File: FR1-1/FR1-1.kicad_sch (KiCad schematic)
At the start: 32 parts

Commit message: cleaning up references
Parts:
- renumbered 1A_FR1_ to 1A_FR1, 1A_FR2_ to 1A_FR2, 1B_FR1_ to 1B_FR1, 1B_FR2_ to 1B_FR2, 1C_FR1_ to 1C_FR1, 1C_FR2_ to 1C_FR2, 1D_FR1_ to 1D_FR1, 1D_FR2_ to 1D_FR2, 1E_FR1_ to 1E_FR1, 1E_FR2_ to 1E_FR2, 3A_FR1_ to 3A_FR1, 3A_FR2_ to 3A_FR2, 3B_FR1_ to 3B_FR1, 3B_FR2_ to 3B_FR2, 3C_FR1_ to 3C_FR1, 3C_FR2_ to 3C_FR2, 3E_FR1_ to 3E_FR1, 3E_FR2_ to 3E_FR2, 3F_FR1_ to 3F_FR1, 3F_FR2_ to 3F_FR2, 5A_FR1_1 to 5A_FR1, 5A_FR2_ to 5A_FR2, 5B_FR1_1 to 5B_FR1, 5B_FR2_ to 5B_FR2, 5C_FR1_1 to 5C_FR1, 5C_FR2_ to 5C_FR2, 5E_FR1_ to 5E_FR1, 5E_FR2_ to 5E_FR2, 5F_FR1_ to 5F_FR1, 5F_FR2_ to 5F_FR2

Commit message: Some initial fixing of ERC errors.
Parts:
- added unit 2 of 5A_FR1
- added unit 2 of 5B_FR1
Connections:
- net GND: now also 5A_FR1.7 (GND), 5B_FR1.7 (GND)
- net VCC: now also 5A_FR1.14 (VCC), 5B_FR1.14 (VCC)

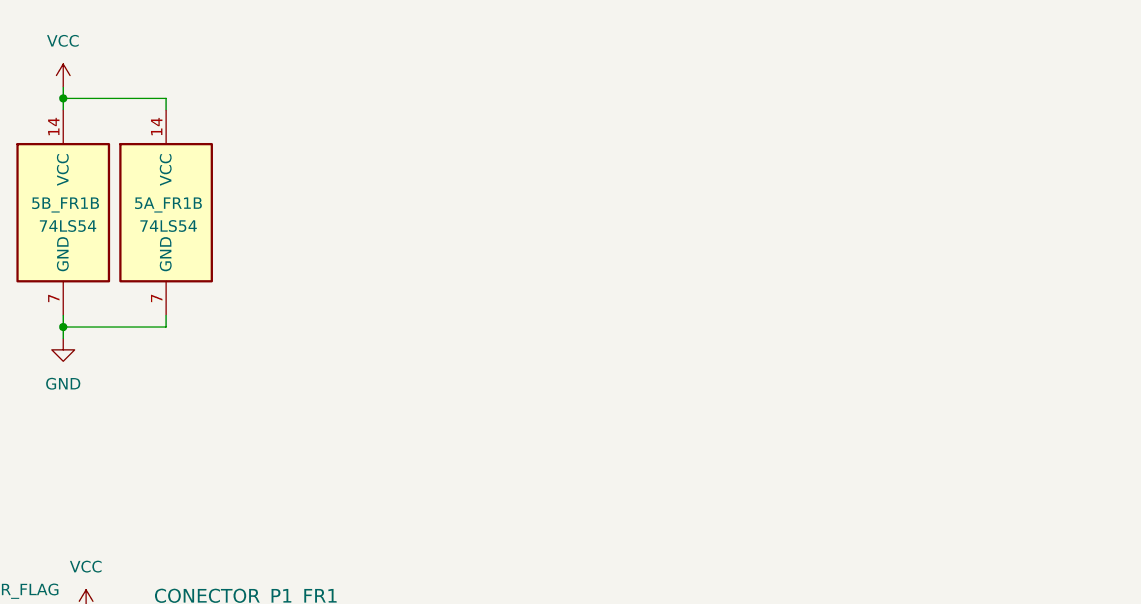
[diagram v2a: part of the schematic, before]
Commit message: addressing a few more ERC errors
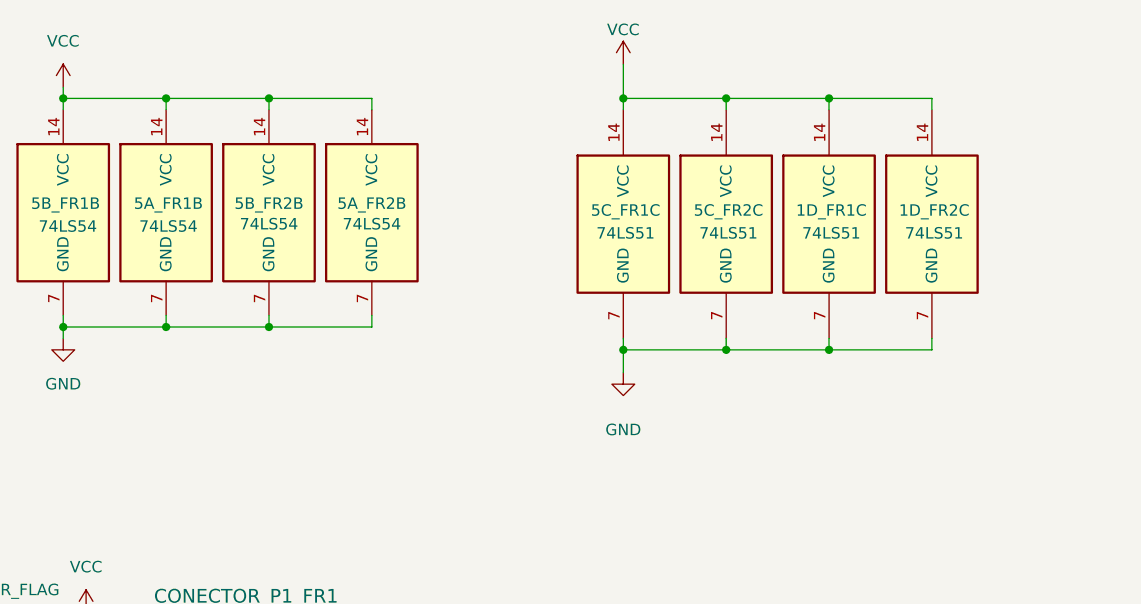
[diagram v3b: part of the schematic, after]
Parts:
- added unit 3 of 1D_FR1
- added unit 3 of 1D_FR2
- added unit 2 of 5A_FR2
- added unit 2 of 5B_FR2
- added unit 3 of 5C_FR1
- added unit 3 of 5C_FR2
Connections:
- net GND: now also 1D_FR1.7 (GND), 1D_FR2.7 (GND), 5A_FR2.7 (GND), 5B_FR2.7 (GND), 5C_FR1.7 (GND), 5C_FR2.7 (GND)
- net VCC: now also 1D_FR1.14 (VCC), 1D_FR2.14 (VCC), 5A_FR2.14 (VCC), 5B_FR2.14 (VCC), 5C_FR1.14 (VCC), 5C_FR2.14 (VCC)

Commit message: fix a whole bunch of errors
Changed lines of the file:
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@@
 	)
 	(junction
-		(at 45.72 22.86)
-		(diameter 0)
-		(color 0 0 0 0)
-	)
-	(junction
 		(at 217.17 157.48)
 		(diameter 0)
@@
 	(wire
 		(pts
-			(xy 38.1 22.86) (xy 45.72 22.86)
-		)
-		(stroke
-			(width 0)
-			(type default)
-		)
-	)
-	(wire
-		(pts
 			(xy 298.45 125.73) (xy 298.45 93.98)
 		)
@@
 	(wire
 		(pts
-			(xy 38.1 21.59) (xy 38.1 22.86)
-		)
-		(stroke
-			(width 0)
-			(type default)
-		)
-	)
-	(wire
-		(pts
 			(xy 374.65 66.04) (xy 374.65 83.82)
 		)
@@
 					(unit 1)
 				)
-			)
-		)
-	)
-	(symbol
-		(lib_id "power:PWR_FLAG")
-		(at 38.1 21.59 0)
-		(unit 1)
-		(body_style 1)
-		(exclude_from_sim no)
-		(in_bom yes)
-		(on_board yes)
-		(in_pos_files yes)
-		(dnp no)
-		(fields_autoplaced yes)
-		(property "Reference" "#FLG07"
-			(at 38.1 19.685 0)
-			(hide yes)
-			(show_name no)
-			(do_not_autoplace no)
-			(effects
-				(font
-					(size 1.27 1.27)
-				)
-			)
-		)
-		(property "Value" "PWR_FLAG"
-			(at 38.1 16.51 0)
-			(show_name no)
-			(do_not_autoplace no)
-			(effects
-				(font
-					(size 1.27 1.27)
-				)
-			)
-		)
-		(property "Footprint" ""
-			(at 38.1 21.59 0)
-			(hide yes)
-			(show_name no)
-			(do_not_autoplace no)
-			(effects
-				(font
-					(size 1.27 1.27)
-				)
-			)
-		)
-		(property "Datasheet" ""
-			(at 38.1 21.59 0)
-			(hide yes)
-			(show_name no)
-			(do_not_autoplace no)
-			(effects
-				(font
-					(size 1.27 1.27)
-				)
-			)
-		)
-		(property "Description" "Special symbol for telling ERC where power comes from"
-			(at 38.1 21.59 0)
-			(hide yes)
-			(show_name no)
-			(do_not_autoplace no)
-			(effects
-				(font
-					(size 1.27 1.27)
-				)
-			)
-		)
-		(pin "1"
-		)
-		(instances
-			(project "patinhofeio"
-				(path "/aca06203-542d-4682-a7e3-8839e24cce95/b383f260-e697-4084-9247-6984c2eebf73"
-					(reference "#FLG07")
-					(unit 1)
-				)

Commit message: melhorias dessa semana
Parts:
- removed 1E_FR1, 1E_FR2: 7400, Housings_DIP:DIP-14_W7.62mm_Socket_LongPads, symbol CDE-3-rescue:7400-RESCUE-CDE-3
- removed 3E_FR1, 3E_FR2, 3F_FR1, 3F_FR2, 5E_FR1, 5E_FR2, 5F_FR1, 5F_FR2: 74HC74, symbol CCE-2-rescue:74HC74
- added 1E_FR1, 1E_FR2: 74LS00, symbol 74xx:74LS00
- added 3E_FR1, 3E_FR2, 3F_FR1, 3F_FR2, 5E_FR1, 5E_FR2, 5F_FR1, 5F_FR2: 74LS74, symbol 74xx:74LS74
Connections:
- net -I0: now also 1E_FR1.3
- net -I1: now also 1E_FR2.3
- net -I2: now also 1E_FR1.6
- net -I3: now also 1E_FR2.6
- net -I4: now also 1E_FR1.11
- net -I5: now also 1E_FR2.11
- net -I6: now also 1E_FR1.8
- net -I7: now also 1E_FR2.8
- net -R0b: now also 3F_FR1.2 (D), 5F_FR1.2 (D)
- net -R1b: now also 3F_FR2.2 (D), 5F_FR2.2 (D)
- net -R2b: now also 3F_FR1.12 (D), 5F_FR1.12 (D)
- net -R3b: now also 3F_FR2.12 (D), 5F_FR2.12 (D)
- net -R4b: now also 3E_FR1.2 (D), 5E_FR1.2 (D)
- net -R5b: now also 3E_FR2.2 (D), 5E_FR2.2 (D)
- net -R6b: now also 3E_FR1.12 (D), 5E_FR1.12 (D)
- net -R7b: now also 3E_FR2.12 (D), 5E_FR2.12 (D)
- net C-RD: now also 3E_FR1.11 (C), 3E_FR1.3 (C), 3E_FR2.11 (C), 3E_FR2.3 (C), 3F_FR1.11 (C), 3F_FR1.3 (C), 3F_FR2.11 (C), 3F_FR2.3 (C)
- net C-RI: now also 5E_FR1.11 (C), 5E_FR1.3 (C), 5E_FR2.11 (C), 5E_FR2.3 (C), 5F_FR1.11 (C), 5F_FR1.3 (C), 5F_FR2.11 (C), 5F_FR2.3 (C)
- net CLEAR: now also 5E_FR1.1 (~{R}), 5E_FR1.13 (~{R}), 5E_FR2.1 (~{R}), 5E_FR2.13 (~{R}), 5F_FR1.1 (~{R}), 5F_FR1.13 (~{R}), 5F_FR2.1 (~{R}), 5F_FR2.13 (~{R})
- net GND: now also 1E_FR1.7 (GND), 1E_FR2.7 (GND), 3E_FR1.7 (GND), 3E_FR2.7 (GND), 3F_FR1.7 (GND), 3F_FR2.7 (GND), 5E_FR1.7 (GND), 5E_FR2.7 (GND), 5F_FR1.7 (GND), 5F_FR2.7 (GND)
- net RD0: now also 3F_FR1.6 (~{Q})
- net RD1: now also 3F_FR2.6 (~{Q})
- net RD2: now also 3F_FR1.8 (~{Q})
- net RD3: now also 3F_FR2.8 (~{Q})
- net RD4: now also 3E_FR1.6 (~{Q})
- net RD5: now also 3E_FR2.6 (~{Q})
- net RD6: now also 3E_FR1.8 (~{Q})
- net RD7: now also 3E_FR2.8 (~{Q})
- net RE0: now also 1E_FR1.2
- net RE1: now also 1E_FR2.2
- net RE2: now also 1E_FR1.5
- net RE3: now also 1E_FR2.5
- net RE4: now also 1E_FR1.12
- net RE5: now also 1E_FR2.12
- net RE6: now also 1E_FR1.9
- net RE7: now also 1E_FR2.9
- net RE/I: now also 1E_FR1.1, 1E_FR1.10, 1E_FR1.13, 1E_FR1.4, 1E_FR2.1, 1E_FR2.10, 1E_FR2.13, 1E_FR2.4
- net RI0: now also 5F_FR1.6 (~{Q})
- net RI1: now also 5F_FR2.6 (~{Q})
- net RI2: now also 5F_FR1.8 (~{Q})
- net RI3: now also 5F_FR2.8 (~{Q})
- net RI4: now also 5E_FR1.6 (~{Q})
- net RI5: now also 5E_FR2.6 (~{Q})
- net RI6: now also 5E_FR1.8 (~{Q})
- net RI7: now also 5E_FR2.8 (~{Q})
- net VCC: now also 1E_FR1.14 (VCC), 1E_FR2.14 (VCC), 3E_FR1.14 (VCC), 3E_FR2.14 (VCC), 3F_FR1.14 (VCC), 3F_FR2.14 (VCC), 5E_FR1.14 (VCC), 5E_FR2.14 (VCC), 5F_FR1.14 (VCC), 5F_FR2.14 (VCC)
